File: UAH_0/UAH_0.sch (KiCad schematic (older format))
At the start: 19 parts, among them X1 Check_point, X2 Check_point, X3 LOGO_NIKITOS_19х7, X5 Клеммник_х2_KLS2-300-5.00-02P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, X6 Клеммник_х2_KLS2-300-5.00-02P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, X7 Клеммник_х2_KLS2-300-5.00-02P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, X8 Клеммник_х2_KLS2-300-5.00-02P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

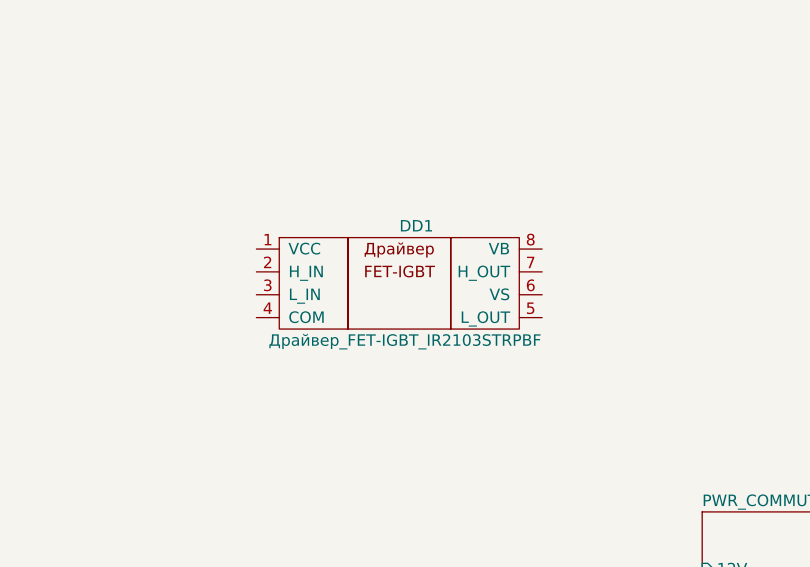
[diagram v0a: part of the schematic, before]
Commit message: обновлена схема управления движками
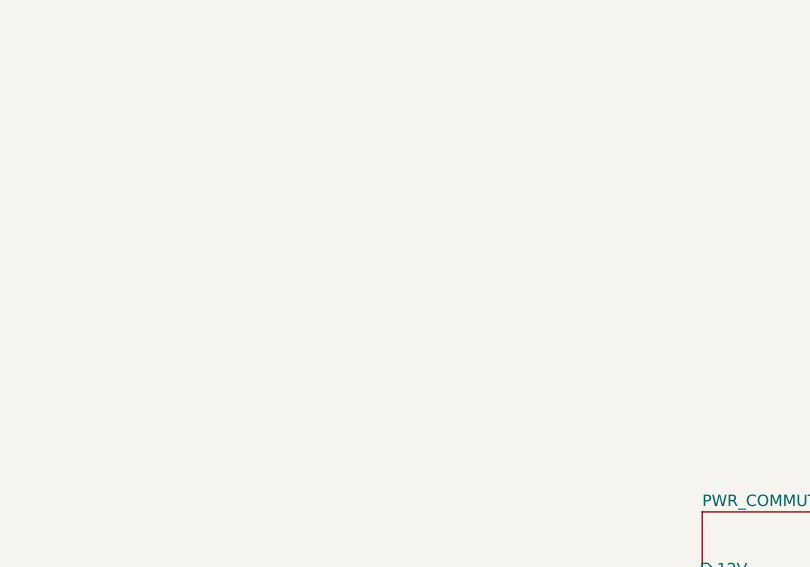
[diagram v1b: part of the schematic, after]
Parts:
- removed DD1: Драйвер_FET-IGBT_IR2103STRPBF, N_DD:SO-8, symbol elements_2020:Драйвер_FET-IGBT_IR2103STRPBF
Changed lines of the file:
@@
 EESchema Schematic File Version 4
+LIBS:UAH_0-cache
 EELAYER 30 0
 EELAYER END
@@
 	1    0    0    -1
 $EndComp
-$Comp
-L elements_2020:Драйвер_FET-IGBT_IR2103STRPBF DD1
-U 1 1 5F2F1BBD
-P 8550 4850
-F 0 "DD1" H 9250 4950 50  0000 C CNN
-F 1 "Драйвер_FET-IGBT_IR2103STRPBF" H 9200 4450 50  0000 C CNN
-F 2 "N_DD:SO-8" H 8550 4850 50  0001 C CNN
-F 3 "" H 8550 4850 50  0001 C CNN
-	1    8550 4850
-	1    0    0    -1
-$EndComp

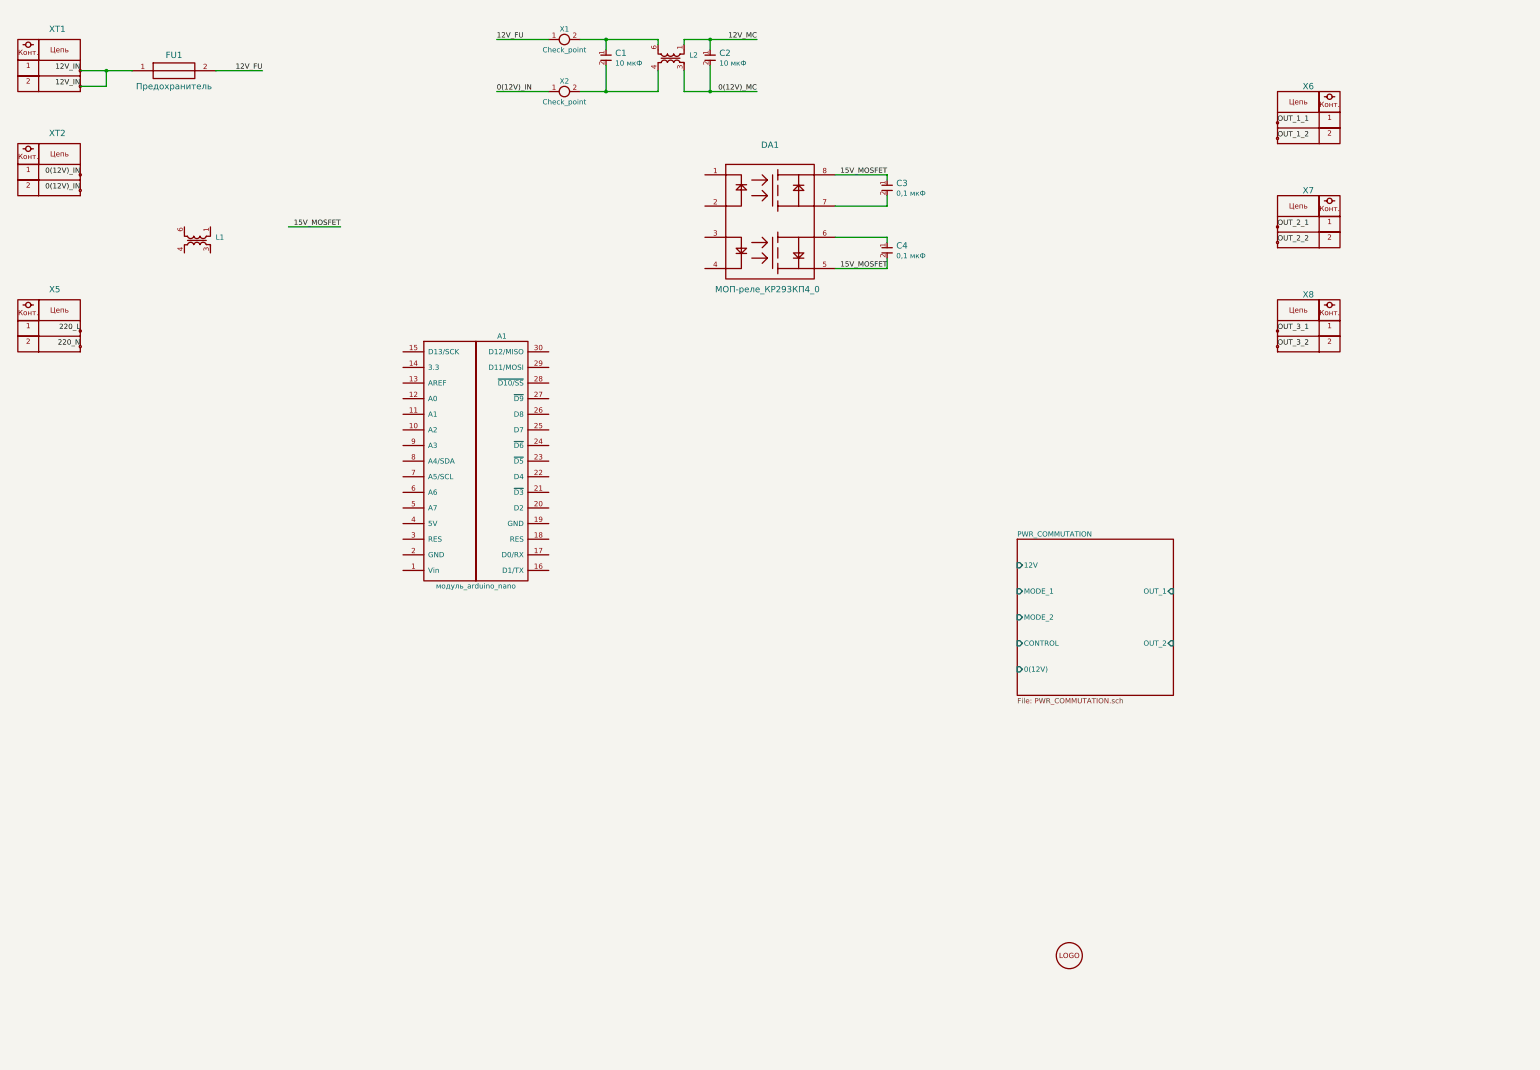
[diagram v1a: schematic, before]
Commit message: закончена принципиальная схема, подготовлен мост и обвес на 1й канал
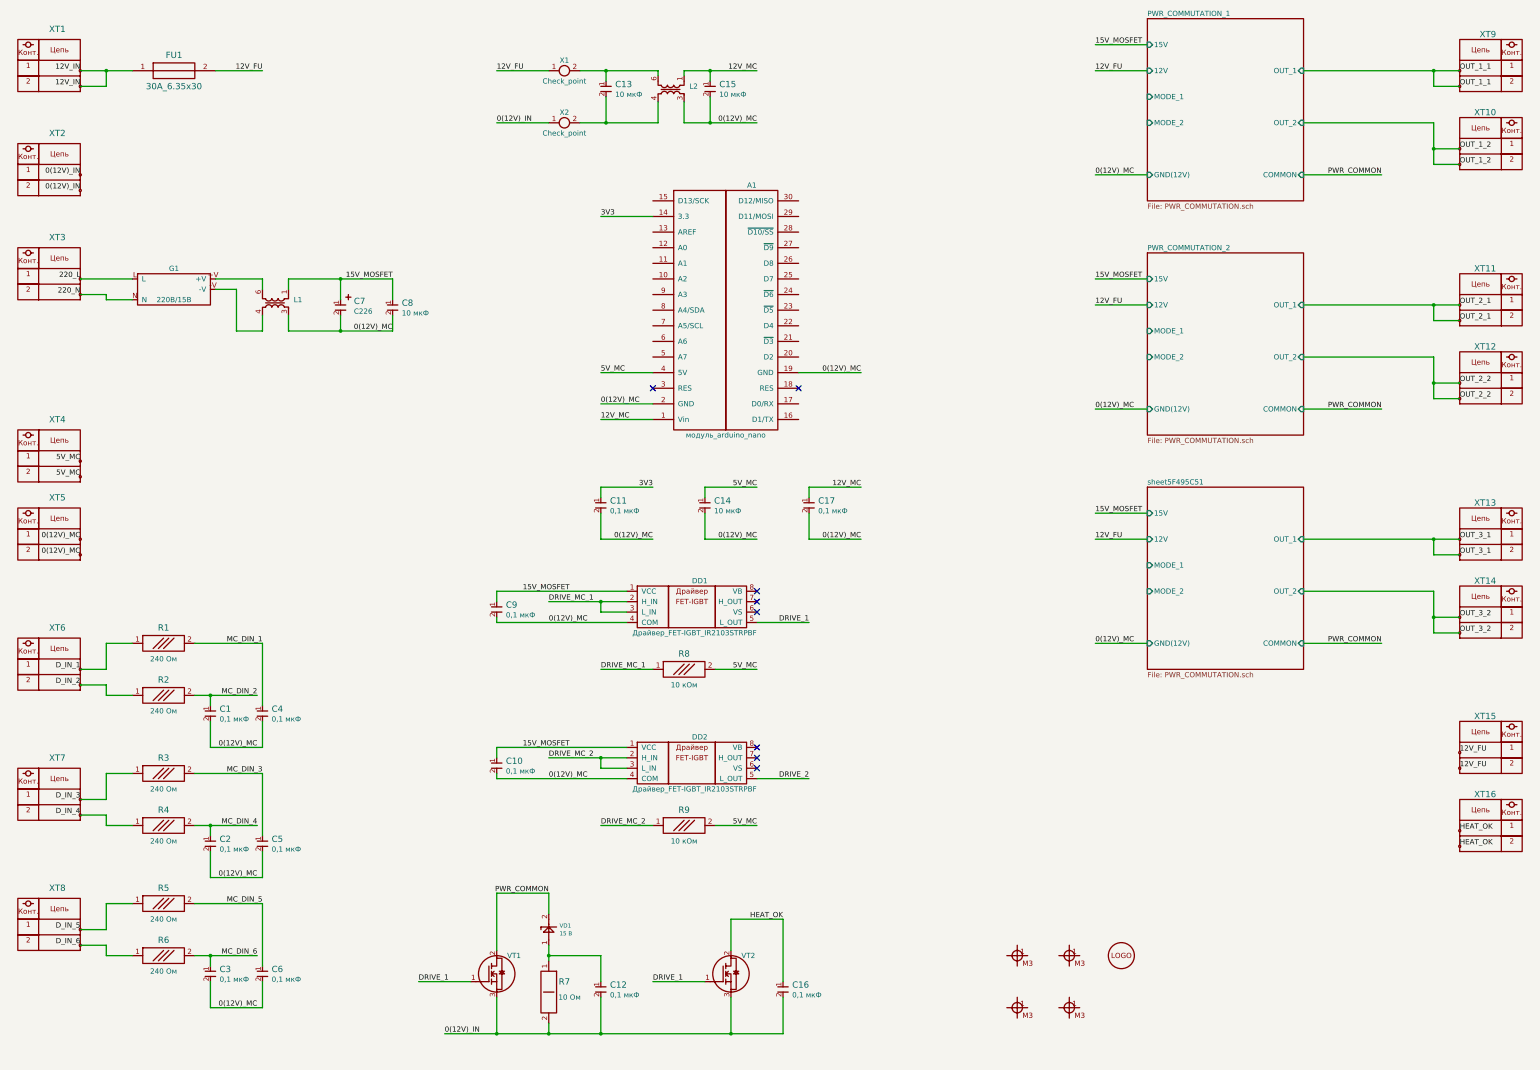
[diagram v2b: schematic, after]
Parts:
- removed DA1: МОП-реле_КР293КП4_0, symbol elements:МОП-реле_КР293КП4_0
- added C1, C10, C11, C12, C16, C17, C2, C5, C6, C9: Конденсатор_16В_0.1_мкФ+-10проц., MOTOR_RLC:Конденсатор_SMD_К10-83(0603), symbol MOTOR_2020_import:Конденсатор_16В_0.1_мкФ+-10проц.
- added C14, C8: Конденсатор_16В_10_мкФ+-10проц., MOTOR_RLC:Конденсатор_SMD_0805, symbol MOTOR_2020_import:Конденсатор_16В_10_мкФ+-10проц.
- added C7: Конденсатор_К53-56А-32В-22_мкФ+-10проц., MOTOR_RLC:Конденсатор_тантал_SMD_m7343, symbol MOTOR_2020_components:Конденсатор_К53-56А-32В-22_мкФ+-10проц.
- added DD1, DD2: Драйвер_FET-IGBT_IR2103STRPBF, N_DD:SO-8, symbol elements_2020:Драйвер_FET-IGBT_IR2103STRPBF
- added G1: AC-DC-преобразователь_IRM-10-15, N_G:AC-DC_IRM-10-15, symbol elements_2020:AC-DC-преобразователь_IRM-10-15
- added R1, R2, R3, R4, R5, R6: Резистор_Р1-12-0,1_ум.-240_Ом±5%-Н-«А», MOTOR_RLC:Резистор_SMD_0603-0,075_Вт, symbol MOTOR_2020_components:Резистор_Р1-12-0,1_ум.-240_Ом±5%-Н-«А»
- added R7: Резистор_CF-100_10_Ом_1Вт, N_RLC:резистор_C1-4-1_Вт_вертикальный, symbol elements:Резистор_1Вт
- added R8, R9: Резистор_10_кОм±5%_0,1Вт, MOTOR_RLC:Резистор_SMD_0603-0,075_Вт, symbol MOTOR_2020_import:Резистор_10_кОм±5%_0,1Вт
- added VD1: Стабилитрон_1N5352BRLG_вертикальный, N_VD_HL:стабилитрон_DO-201_вертикальный, symbol elements_2020:Стабилитрон_1N5352BRLG_вертикальный
- added VT1, VT2: MOSFET_N-канал_AUIRF3205Z, N_VD_HL:Транзистор_N_STP10NK60Z, symbol elements_2020:MOSFET_N-канал_AUIRF3205Z
- added X3, X4, X5, X6: Крепежное_отверстие_М3, MOTOR_ICO:Крепежное_Отверстие_под_М3, symbol MOTOR_2020_components:Крепежное_отверстие_М3
- added XT10, XT13, XT14, XT15, XT16, XT4, XT5, XT6, XT7, XT8: Клеммник_х2_KLS2-300-5.00-02P-2S, N_X:Клеммник_х2_шаг5, symbol elements_2020:Клеммник_х2_KLS2-300-5.00-02P-2S
- FU1: value Предохранитель -> 30А_6.35х30; footprint (none) -> N_RLC:Предохранитель_6.35x30
- XT11: renamed from X7; footprint (none) -> N_X:Клеммник_х2_шаг5
- XT12: renamed from X8; footprint (none) -> N_X:Клеммник_х2_шаг5
- XT9: renamed from X6; footprint (none) -> N_X:Клеммник_х2_шаг5
- renumbered C1 to C13, C2 to C15, X3 to X7, X5 to XT3
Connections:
- net labels added: 3V3, 5V_MC, DRIVE_1, DRIVE_2, DRIVE_MC_1, DRIVE_MC_2, D_IN_1, D_IN_2, D_IN_3, D_IN_4, D_IN_5, D_IN_6, HEAT_OK, MC_DIN_1, MC_DIN_2, MC_DIN_3, MC_DIN_4, MC_DIN_5, MC_DIN_6, PWR_COMMON
- wire segments 32 -> 185
- no-connect marks 0 -> 8
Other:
- moved on the sheet: A1, C13, C15, L1, L2, X1, X2, XT11, XT12, XT3, XT9

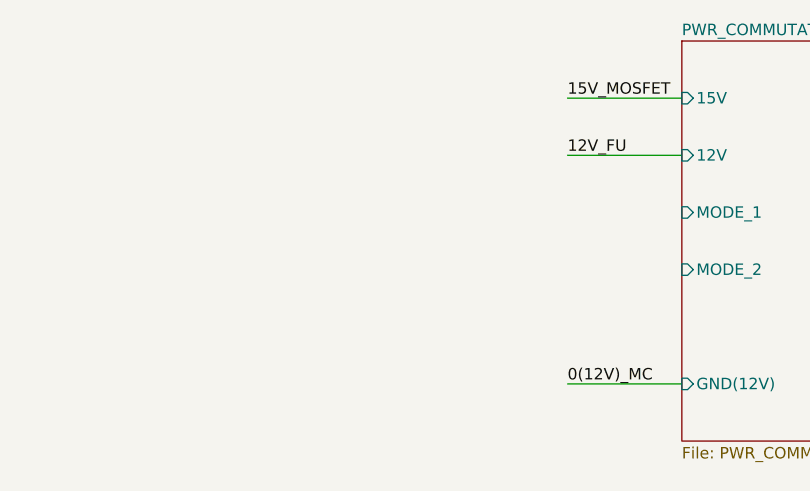
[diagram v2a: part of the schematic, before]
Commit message: расставлена силовая часть на 3 канала, нет управления и главных ключей
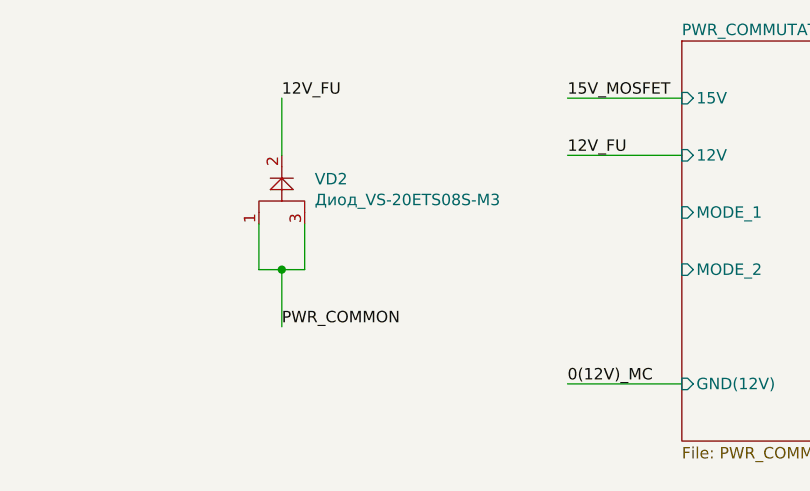
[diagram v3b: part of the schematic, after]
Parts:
- added VD2: Диод_VS-20ETS08S-M3, N_VD_HL:Транзистор_N-канал_dpak, symbol elements_2020:Диод_VS-20ETS08S-M3
- VT1, VT2: footprint N_VD_HL:Транзистор_N_STP10NK60Z -> N_VD_HL:Транзистор_TO-220_COOLING
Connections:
- net 12V_FU: now also VD2.2
- net PWR_COMMON: now also VD2.1, VD2.3
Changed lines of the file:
@@
 F 0 "VT1" H 5600 10200 50  0000 L CNN
 F 1 "MOSFET_N-канал_AUIRF3205Z" H 5703 9980 50  0001 L CNN
-F 2 "N_VD_HL:Транзистор_N_STP10NK60Z" H 5600 9550 50  0001 C CNN
+F 2 "N_VD_HL:Транзистор_TO-220_COOLING" H 5600 9550 50  0001 C CNN
 F 3 "" H 5450 10100 50  0001 C CNN
 F 4 "" H 5450 10100 50  0001 C CNN "LINK"
@@
 F 0 "VT2" H 7850 10200 50  0000 L CNN
 F 1 "MOSFET_N-канал_AUIRF3205Z" H 7953 9980 50  0001 L CNN
-F 2 "N_VD_HL:Транзистор_N_STP10NK60Z" H 7850 9550 50  0001 C CNN
+F 2 "N_VD_HL:Транзистор_TO-220_COOLING" H 7850 9550 50  0001 C CNN
 F 3 "" H 7700 10100 50  0001 C CNN
 F 4 "" H 7700 10100 50  0001 C CNN "LINK"
@@
 Wire Wire Line
 	2800 3500 3250 3500
+$Comp
+L elements_2020:Диод_VS-20ETS08S-M3 VD?
+U 1 1 5F3B01BC
+P 9900 1800
+AR Path="/5F33B5F7/5F3B01BC" Ref="VD?"  Part="1"
+AR Path="/5F48FE9A/5F3B01BC" Ref="VD?"  Part="1"
+AR Path="/5F495C51/5F3B01BC" Ref="VD?"  Part="1"
+AR Path="/5F3B01BC" Ref="VD2"  Part="1"
+F 0 "VD2" H 10144 1996 50  0000 L CNN
+F 1 "Диод_VS-20ETS08S-M3" H 10144 1905 50  0000 L CNN
+F 2 "N_VD_HL:Транзистор_N-канал_dpak" H 10225 1600 50  0001 C CNN
+F 3 "" V 9900 1700 50  0001 C CNN
+	1    9900 1800
+	1    0    0    -1
+$EndComp
+Text Label 10000 2250 0    50   ~ 0
+PWR_COMMON
+Text Label 10000 1250 0    50   ~ 0
+12V_FU
+Wire Wire Line
+	10000 1250 10000 1500
+Wire Wire Line
+	9900 1800 9900 2000
+Wire Wire Line
+	9900 2000 10000 2000
+Wire Wire Line
+	10100 2000 10100 1800
+Wire Wire Line
+	10000 2000 10000 2250
+Connection ~ 10000 2000
+Wire Wire Line
+	10000 2000 10100 2000
 $EndSCHEMATC
